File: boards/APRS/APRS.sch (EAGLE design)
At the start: 15 parts

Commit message: First pass of APRS v2
- Cleaned up the board (removed unnecessary things)
- Switched to using more library objects
- Switched to TPS6300x for power
- Integrated the Venus GPS
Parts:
- LED1: device SparkFun:LED3MM -> SparkFun-LED:LED0603
- R1, R_T0, R_T1, R_T2: device SparkFun:RESISTORAXIAL-0.3 -> SparkFun-Passives:RESISTOR0805-RES
- renumbered POWER1 to POWER5, POWER2 to POWER3
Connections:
- new net 3.3V_EN: ARDUINO.D10*, POWER3.EN
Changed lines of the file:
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@@
 <?xml version="1.0" encoding="utf-8"?>
 <!DOCTYPE eagle SYSTEM "eagle.dtd">
-<eagle version="6.1">
+<eagle version="6.2">
 <drawing>
 <settings>
@@
 <parts>
 <part name="J$1" library="SparkFun" deviceset="SMA_EDGE" device=""/>
-<part name="R_T2" library="SparkFun" deviceset="RESISTOR" device="AXIAL-0.3" value="10k"/>
-<part name="R_T1" library="SparkFun" deviceset="RESISTOR" device="AXIAL-0.3" value="10k"/>
-<part name="LED1" library="SparkFun" deviceset="LED" device="3MM"/>
-<part name="R1" library="SparkFun" deviceset="RESISTOR" device="AXIAL-0.3" value="330"/>
+<part name="R_T2" library="SparkFun-Passives" deviceset="RESISTOR" device="0805-RES" value="10k"/>
+<part name="R_T1" library="SparkFun-Passives" deviceset="RESISTOR" device="0805-RES" value="10k"/>
+<part name="LED1" library="SparkFun-LED" deviceset="LED" device="0603"/>
+<part name="R1" library="SparkFun-Passives" deviceset="RESISTOR" device="0805-RES" value="330"/>
 <part name="U$1" library="SparkFun-Aesthetics" deviceset="5V" device=""/>
 <part name="P+1" library="SparkFun-Aesthetics" deviceset="3.3V" device=""/>
@@
 <part name="GND6" library="SparkFun-Aesthetics" deviceset="GND" device=""/>
 <part name="GND7" library="SparkFun-Aesthetics" deviceset="GND" device=""/>
-<part name="R_T0" library="SparkFun" deviceset="RESISTOR" device="AXIAL-0.3" value="10k"/>
+<part name="R_T0" library="SparkFun-Passives" deviceset="RESISTOR" device="0805-RES" value="10k"/>
 <part name="THERM0" library="SparkFun" deviceset="M02" device="PTH"/>
 <part name="U$6" library="SparkFun-Aesthetics" deviceset="5V" device=""/>
@@
 <part name="THERM1" library="SparkFun-Connectors" deviceset="M02" device="JST-PTH-2"/>
 <part name="THERM2" library="SparkFun-Connectors" deviceset="M02" device="JST-PTH-2"/>
-<part name="POWER1" library="OpenSpace" deviceset="POWER" device="-TPS6300X" value="5V"/>
-<part name="POWER2" library="OpenSpace" deviceset="POWER" device="-TPS6300X" value="3.3V"/>
 <part name="RADIOMETRIX_HX1" library="OpenSpace" deviceset="RADIOMETRIX-HX1" device=""/>
 <part name="LEVEL_SHIFT" library="OpenSpace" deviceset="SN74LVC1T45" device="-DCK"/>
@@
 <part name="U$10" library="SparkFun-Aesthetics" deviceset="5V" device=""/>
 <part name="P+3" library="SparkFun-Aesthetics" deviceset="3.3V" device=""/>
+<part name="POWER5" library="OpenSpace" deviceset="POWER" device="-TPS6300X" value="5V"/>
+<part name="POWER3" library="OpenSpace" deviceset="POWER" device="-TPS6300X" value="3.3V"/>
 </parts>
 <sheets>
@@
 <instance part="GND1" gate="1" x="17.78" y="50.8"/>
 <instance part="GND2" gate="1" x="76.2" y="50.8"/>
-<instance part="U$2" gate="G$1" x="22.86" y="91.44"/>
+<instance part="U$2" gate="G$1" x="22.86" y="96.52"/>
 <instance part="GPS0" gate="G$1" x="256.54" y="22.86"/>
 <instance part="GND3" gate="1" x="99.06" y="10.16"/>
@@
 <instance part="THERM1" gate="G$1" x="218.44" y="76.2"/>
 <instance part="THERM2" gate="G$1" x="243.84" y="76.2"/>
-<instance part="POWER1" gate="POWER" x="48.26" y="83.82"/>
-<instance part="POWER2" gate="POWER" x="48.26" y="63.5"/>
 <instance part="RADIOMETRIX_HX1" gate="RADIOMETRIX-HX1_$1" x="43.18" y="33.02"/>
 <instance part="LEVEL_SHIFT" gate="G$1" x="205.74" y="25.4"/>
@@
 <instance part="U$10" gate="G$1" x="187.96" y="40.64"/>
 <instance part="P+3" gate="G$1" x="223.52" y="40.64"/>
+<instance part="POWER5" gate="POWER" x="48.26" y="83.82"/>
+<instance part="POWER3" gate="POWER" x="48.26" y="63.5"/>
 </instances>
 <busses>
@@
 </segment>
 <segment>
-<wire x1="30.48" y1="81.28" x2="17.78" y2="81.28" width="0.1524" layer="91"/>
-<wire x1="17.78" y1="81.28" x2="17.78" y2="60.96" width="0.1524" layer="91"/>
-<wire x1="17.78" y1="60.96" x2="17.78" y2="53.34" width="0.1524" layer="91"/>
-<wire x1="30.48" y1="60.96" x2="17.78" y2="60.96" width="0.1524" layer="91"/>
-<junction x="17.78" y="60.96"/>
+<wire x1="30.48" y1="78.74" x2="17.78" y2="78.74" width="0.1524" layer="91"/>
+<wire x1="17.78" y1="78.74" x2="17.78" y2="58.42" width="0.1524" layer="91"/>
+<wire x1="17.78" y1="58.42" x2="17.78" y2="53.34" width="0.1524" layer="91"/>
+<wire x1="30.48" y1="58.42" x2="17.78" y2="58.42" width="0.1524" layer="91"/>
+<junction x="17.78" y="58.42"/>
 <pinref part="GND1" gate="1" pin="GND"/>
-<pinref part="POWER1" gate="POWER" pin="BATT-"/>
-<pinref part="POWER2" gate="POWER" pin="BATT-"/>
+<pinref part="POWER5" gate="POWER" pin="BATT-"/>
+<pinref part="POWER3" gate="POWER" pin="BATT-"/>
 </segment>
 <segment>
@@
 <junction x="76.2" y="60.96"/>
 <pinref part="GND2" gate="1" pin="GND"/>
-<pinref part="POWER1" gate="POWER" pin="VCC-"/>
-<pinref part="POWER2" gate="POWER" pin="VCC-"/>
+<pinref part="POWER5" gate="POWER" pin="VCC-"/>
+<pinref part="POWER3" gate="POWER" pin="VCC-"/>
 </segment>
 <segment>
@@
 <wire x1="71.12" y1="86.36" x2="71.12" y2="91.44" width="0.1524" layer="91"/>
 <pinref part="U$1" gate="G$1" pin="5V"/>
-<pinref part="POWER1" gate="POWER" pin="VCC+"/>
+<pinref part="POWER5" gate="POWER" pin="VCC+"/>
 </segment>
 <segment>
@@
 <wire x1="71.12" y1="66.04" x2="71.12" y2="71.12" width="0.1524" layer="91"/>
 <pinref part="P+1" gate="G$1" pin="3.3V"/>
-<pinref part="POWER2" gate="POWER" pin="VCC+"/>
+<pinref part="POWER3" gate="POWER" pin="VCC+"/>
 </segment>
 <segment>
@@
 <net name="1.8V" class="0">
 <segment>
-<wire x1="30.48" y1="66.04" x2="22.86" y2="66.04" width="0.1524" layer="91"/>
-<wire x1="30.48" y1="86.36" x2="22.86" y2="86.36" width="0.1524" layer="91"/>
-<wire x1="22.86" y1="86.36" x2="22.86" y2="91.44" width="0.1524" layer="91"/>
-<wire x1="22.86" y1="66.04" x2="22.86" y2="86.36" width="0.1524" layer="91"/>
-<junction x="22.86" y="86.36"/>
+<wire x1="30.48" y1="63.5" x2="22.86" y2="63.5" width="0.1524" layer="91"/>
+<wire x1="30.48" y1="83.82" x2="22.86" y2="83.82" width="0.1524" layer="91"/>
+<wire x1="22.86" y1="83.82" x2="22.86" y2="96.52" width="0.1524" layer="91"/>
+<wire x1="22.86" y1="63.5" x2="22.86" y2="83.82" width="0.1524" layer="91"/>
+<junction x="22.86" y="83.82"/>
 <pinref part="U$2" gate="G$1" pin="1.8V"/>
-<pinref part="POWER1" gate="POWER" pin="BATT+"/>
-<pinref part="POWER2" gate="POWER" pin="BATT+"/>
+<pinref part="POWER5" gate="POWER" pin="BATT+"/>
+<pinref part="POWER3" gate="POWER" pin="BATT+"/>
 </segment>
 <segment>
@@
 </segment>
 </net>
+<net name="3.3V_EN" class="0">
+<segment>
+<pinref part="POWER3" gate="POWER" pin="EN"/>
+<wire x1="30.48" y1="68.58" x2="15.24" y2="68.58" width="0.1524" layer="91"/>
+<label x="15.24" y="68.58" size="1.778" layer="95" rot="MR0"/>
+</segment>
+<segment>
+<pinref part="ARDUINO" gate="G$1" pin="D10*"/>
+<wire x1="152.4" y1="50.8" x2="162.56" y2="50.8" width="0.1524" layer="91"/>
+<label x="162.56" y="50.8" size="1.778" layer="95"/>
+</segment>
+</net>

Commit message: New APRS board, close to ready
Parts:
- added I2C_0: (no value), SparkFun-Connectors:M04PTH
- added I2C_TRANS: PCA9306-D, OpenSpace:PCA9306-D
- added SCL_PU, SDA_PU: 3.3k, SparkFun-Passives:RESISTOR0805-RES
- ARDUINO: value ARDUINO_PRO_MINI -> ARDUINO_PRO_MINI-NOSILK; device OpenSpace:ARDUINO_PRO_MINI -> OpenSpace:ARDUINO_PRO_MINI-NOSILK
- GPS0: value VENUS_GPS -> VENUS_GPS-NOSILK; device OpenSpace:VENUS_GPS -> OpenSpace:VENUS_GPS-NOSILK
- POWER3, POWER5: device OpenSpace:POWER-TPS6300X -> OpenSpace:POWER-TPS6300X-NOSILK
- THERM0: value (none) -> 10k; device SparkFun:M02PTH -> SparkFun-Passives:RESISTOR0805-RES
- THERM1, THERM2: value (none) -> 10k
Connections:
- new net N$4: ARDUINO.A4_SDA, I2C_TRANS.SDA2
- new net N$5: ARDUINO.A5_SCL, I2C_TRANS.SCL2
- new net N$6: ARDUINO.D12, I2C_TRANS.EN
- new net SCL: I2C_0.4, I2C_TRANS.SCL1, SDA_PU.1
- new net SDA: I2C_0.3, I2C_TRANS.SDA1, SCL_PU.1
- net 3.3V: now also I2C_0.2, I2C_TRANS.VREF1, SCL_PU.2, SDA_PU.2
- net 5V: now also I2C_TRANS.VREF2, THERM0.1; no longer THERM0.2
- net A0: now also THERM0.2; no longer THERM0.1
- net GND: now also I2C_0.1, I2C_TRANS.GND
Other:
- moved on the sheet: GPS0, LEVEL_SHIFT, R_T0, R_T1, R_T2, THERM1, THERM2

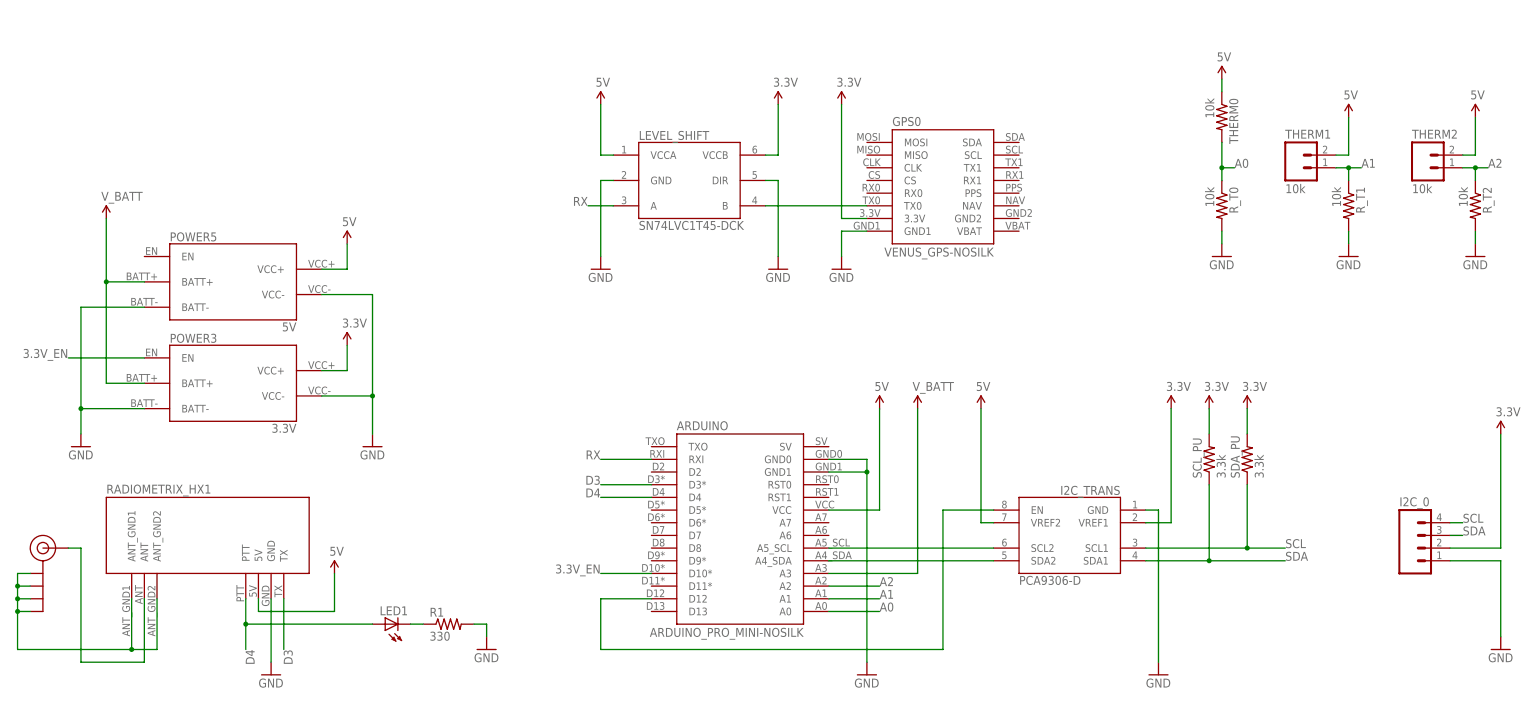
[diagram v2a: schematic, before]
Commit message: Added Jonah receiver to APRS v3
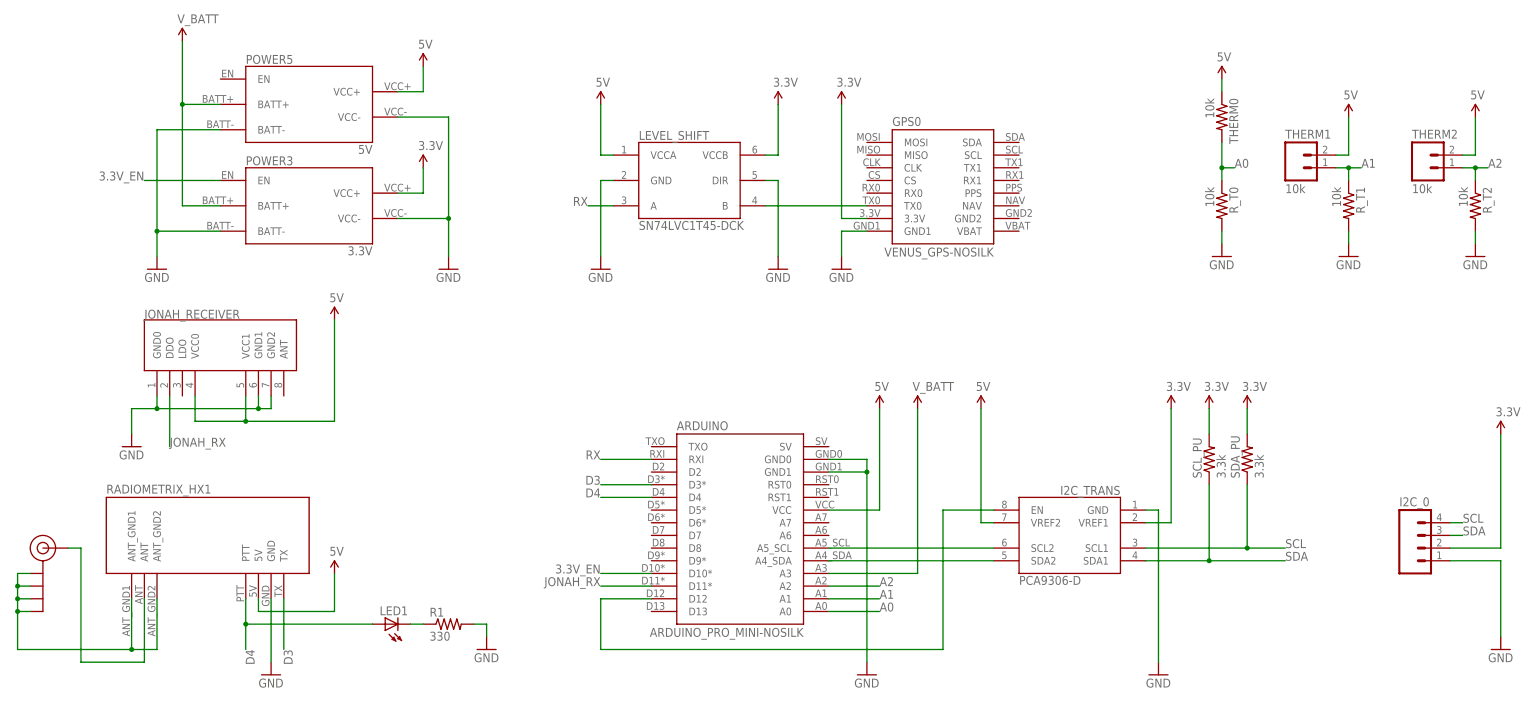
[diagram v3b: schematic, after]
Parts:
- added JONAH_RECEIVER: RADIO-KLP-RECEIVER-NOSILK, OpenSpace:RADIO-KLP-RECEIVER-NOSILK
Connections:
- new net JONAH_RX: ARDUINO.D11*, JONAH_RECEIVER.DDO
- net 5V: now also JONAH_RECEIVER.VCC0, JONAH_RECEIVER.VCC1
- net GND: now also JONAH_RECEIVER.GND0, JONAH_RECEIVER.GND1, JONAH_RECEIVER.GND2
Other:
- moved on the sheet: POWER3, POWER5
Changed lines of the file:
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@@
 <part name="P+9" library="SparkFun-Aesthetics" deviceset="3.3V" device=""/>
 <part name="GND13" library="SparkFun-Aesthetics" deviceset="GND" device=""/>
+<part name="JONAH_RECEIVER" library="OpenSpace" deviceset="RADIO-KLP-RECEIVER" device="-NOSILK"/>
+<part name="GND14" library="SparkFun-Aesthetics" deviceset="GND" device=""/>
+<part name="U$11" library="SparkFun-Aesthetics" deviceset="5V" device=""/>
 </parts>
 <sheets>
@@
 <instance part="LED1" gate="G$1" x="78.74" y="15.24" rot="R90"/>
 <instance part="R1" gate="G$1" x="91.44" y="15.24"/>
-<instance part="U$1" gate="G$1" x="71.12" y="91.44"/>
-<instance part="P+1" gate="G$1" x="71.12" y="71.12"/>
-<instance part="GND1" gate="1" x="17.78" y="50.8"/>
-<instance part="GND2" gate="1" x="76.2" y="50.8"/>
-<instance part="U$2" gate="G$1" x="22.86" y="96.52"/>
+<instance part="U$1" gate="G$1" x="86.36" y="127"/>
+<instance part="P+1" gate="G$1" x="86.36" y="106.68"/>
+<instance part="GND1" gate="1" x="33.02" y="86.36"/>
+<instance part="GND2" gate="1" x="91.44" y="86.36"/>
+<instance part="U$2" gate="G$1" x="38.1" y="132.08"/>
 <instance part="GPS0" gate="G$1" x="190.5" y="101.6"/>
 <instance part="GND3" gate="1" x="99.06" y="10.16"/>
@@
 <instance part="U$10" gate="G$1" x="121.92" y="119.38"/>
 <instance part="P+3" gate="G$1" x="157.48" y="119.38"/>
-<instance part="POWER5" gate="POWER" x="48.26" y="83.82"/>
-<instance part="POWER3" gate="POWER" x="48.26" y="63.5"/>
+<instance part="POWER5" gate="POWER" x="63.5" y="119.38"/>
+<instance part="POWER3" gate="POWER" x="63.5" y="99.06"/>
 <instance part="THERM0" gate="G$1" x="246.38" y="116.84" rot="R270"/>
 <instance part="I2C_TRANS" gate="G$1" x="215.9" y="33.02" rot="MR0"/>
@@
 <instance part="P+9" gate="G$1" x="302.26" y="53.34"/>
 <instance part="GND13" gate="1" x="302.26" y="10.16"/>
+<instance part="JONAH_RECEIVER" gate="G$1" x="45.72" y="71.12"/>
+<instance part="GND14" gate="1" x="27.94" y="50.8"/>
+<instance part="U$11" gate="G$1" x="68.58" y="76.2"/>
 </instances>
 <busses>
@@
 </segment>
 <segment>
-<wire x1="30.48" y1="78.74" x2="17.78" y2="78.74" width="0.1524" layer="91"/>
-<wire x1="17.78" y1="78.74" x2="17.78" y2="58.42" width="0.1524" layer="91"/>
-<wire x1="17.78" y1="58.42" x2="17.78" y2="53.34" width="0.1524" layer="91"/>
-<wire x1="30.48" y1="58.42" x2="17.78" y2="58.42" width="0.1524" layer="91"/>
-<junction x="17.78" y="58.42"/>
+<wire x1="45.72" y1="114.3" x2="33.02" y2="114.3" width="0.1524" layer="91"/>
+<wire x1="33.02" y1="114.3" x2="33.02" y2="93.98" width="0.1524" layer="91"/>
+<wire x1="33.02" y1="93.98" x2="33.02" y2="88.9" width="0.1524" layer="91"/>
+<wire x1="45.72" y1="93.98" x2="33.02" y2="93.98" width="0.1524" layer="91"/>
+<junction x="33.02" y="93.98"/>
 <pinref part="GND1" gate="1" pin="GND"/>
 <pinref part="POWER5" gate="POWER" pin="BATT-"/>
@@
 </segment>
 <segment>
-<wire x1="66.04" y1="81.28" x2="76.2" y2="81.28" width="0.1524" layer="91"/>
-<wire x1="76.2" y1="81.28" x2="76.2" y2="60.96" width="0.1524" layer="91"/>
-<wire x1="76.2" y1="60.96" x2="76.2" y2="53.34" width="0.1524" layer="91"/>
-<wire x1="66.04" y1="60.96" x2="76.2" y2="60.96" width="0.1524" layer="91"/>
-<junction x="76.2" y="60.96"/>
+<wire x1="81.28" y1="116.84" x2="91.44" y2="116.84" width="0.1524" layer="91"/>
+<wire x1="91.44" y1="116.84" x2="91.44" y2="96.52" width="0.1524" layer="91"/>
+<wire x1="91.44" y1="96.52" x2="91.44" y2="88.9" width="0.1524" layer="91"/>
+<wire x1="81.28" y1="96.52" x2="91.44" y2="96.52" width="0.1524" layer="91"/>
+<junction x="91.44" y="96.52"/>
 <pinref part="GND2" gate="1" pin="GND"/>
 <pinref part="POWER5" gate="POWER" pin="VCC-"/>
@@
 <pinref part="GND13" gate="1" pin="GND"/>
 </segment>
+<segment>
+<pinref part="JONAH_RECEIVER" gate="G$1" pin="GND2"/>
+<wire x1="55.88" y1="60.96" x2="55.88" y2="58.42" width="0.1524" layer="91"/>
+<wire x1="55.88" y1="58.42" x2="53.34" y2="58.42" width="0.1524" layer="91"/>
+<wire x1="53.34" y1="58.42" x2="33.02" y2="58.42" width="0.1524" layer="91"/>
+<wire x1="33.02" y1="58.42" x2="27.94" y2="58.42" width="0.1524" layer="91"/>
+<wire x1="27.94" y1="58.42" x2="27.94" y2="53.34" width="0.1524" layer="91"/>
+<pinref part="JONAH_RECEIVER" gate="G$1" pin="GND1"/>
+<wire x1="53.34" y1="60.96" x2="53.34" y2="58.42" width="0.1524" layer="91"/>
+<junction x="53.34" y="58.42"/>
+<pinref part="JONAH_RECEIVER" gate="G$1" pin="GND0"/>
+<wire x1="33.02" y1="60.96" x2="33.02" y2="58.42" width="0.1524" layer="91"/>
+<junction x="33.02" y="58.42"/>
+<pinref part="GND14" gate="1" pin="GND"/>
+</segment>
 </net>
 <net name="RX" class="0">
@@
 </segment>
 <segment>
-<wire x1="66.04" y1="86.36" x2="71.12" y2="86.36" width="0.1524" layer="91"/>
-<wire x1="71.12" y1="86.36" x2="71.12" y2="91.44" width="0.1524" layer="91"/>
+<wire x1="81.28" y1="121.92" x2="86.36" y2="121.92" width="0.1524" layer="91"/>
+<wire x1="86.36" y1="121.92" x2="86.36" y2="127" width="0.1524" layer="91"/>
 <pinref part="U$1" gate="G$1" pin="5V"/>
 <pinref part="POWER5" gate="POWER" pin="VCC+"/>
@@
 <wire x1="198.12" y1="35.56" x2="198.12" y2="58.42" width="0.1524" layer="91"/>
 </segment>
+<segment>
+<pinref part="JONAH_RECEIVER" gate="G$1" pin="VCC0"/>
+<wire x1="40.64" y1="60.96" x2="40.64" y2="55.88" width="0.1524" layer="91"/>
+<wire x1="40.64" y1="55.88" x2="50.8" y2="55.88" width="0.1524" layer="91"/>
+<wire x1="50.8" y1="55.88" x2="68.58" y2="55.88" width="0.1524" layer="91"/>
+<wire x1="68.58" y1="55.88" x2="68.58" y2="76.2" width="0.1524" layer="91"/>
+<pinref part="JONAH_RECEIVER" gate="G$1" pin="VCC1"/>
+<wire x1="50.8" y1="60.96" x2="50.8" y2="55.88" width="0.1524" layer="91"/>
+<junction x="50.8" y="55.88"/>
+<pinref part="U$11" gate="G$1" pin="5V"/>
+</segment>
 </net>
 <net name="N$11" class="0">
@@
 <net name="3.3V" class="0">
 <segment>
-<wire x1="66.04" y1="66.04" x2="71.12" y2="66.04" width="0.1524" layer="91"/>
-<wire x1="71.12" y1="66.04" x2="71.12" y2="71.12" width="0.1524" layer="91"/>
+<wire x1="81.28" y1="101.6" x2="86.36" y2="101.6" width="0.1524" layer="91"/>
+<wire x1="86.36" y1="101.6" x2="86.36" y2="106.68" width="0.1524" layer="91"/>
 <pinref part="P+1" gate="G$1" pin="3.3V"/>
 <pinref part="POWER3" gate="POWER" pin="VCC+"/>
@@
 <net name="1.8V" class="0">
 <segment>
-<wire x1="30.48" y1="63.5" x2="22.86" y2="63.5" width="0.1524" layer="91"/>
-<wire x1="30.48" y1="83.82" x2="22.86" y2="83.82" width="0.1524" layer="91"/>
-<wire x1="22.86" y1="83.82" x2="22.86" y2="96.52" width="0.1524" layer="91"/>
-<wire x1="22.86" y1="63.5" x2="22.86" y2="83.82" width="0.1524" layer="91"/>
-<junction x="22.86" y="83.82"/>
+<wire x1="45.72" y1="99.06" x2="38.1" y2="99.06" width="0.1524" layer="91"/>
+<wire x1="45.72" y1="119.38" x2="38.1" y2="119.38" width="0.1524" layer="91"/>
+<wire x1="38.1" y1="119.38" x2="38.1" y2="132.08" width="0.1524" layer="91"/>
+<wire x1="38.1" y1="99.06" x2="38.1" y2="119.38" width="0.1524" layer="91"/>
+<junction x="38.1" y="119.38"/>
 <pinref part="U$2" gate="G$1" pin="1.8V"/>
 <pinref part="POWER5" gate="POWER" pin="BATT+"/>
@@
 <segment>
 <pinref part="POWER3" gate="POWER" pin="EN"/>
-<wire x1="30.48" y1="68.58" x2="15.24" y2="68.58" width="0.1524" layer="91"/>
-<label x="15.24" y="68.58" size="1.778" layer="95" rot="MR0"/>
+<wire x1="45.72" y1="104.14" x2="30.48" y2="104.14" width="0.1524" layer="91"/>
+<label x="30.48" y="104.14" size="1.778" layer="95" rot="MR0"/>
 </segment>
 <segment>
@@
 </segment>
 </net>
+<net name="JONAH_RX" class="0">
+<segment>
+<pinref part="ARDUINO" gate="G$1" pin="D11*"/>
+<wire x1="132.08" y1="22.86" x2="121.92" y2="22.86" width="0.1524" layer="91"/>
+<label x="121.92" y="22.86" size="1.778" layer="95" rot="MR0"/>
+</segment>
+<segment>
+<pinref part="JONAH_RECEIVER" gate="G$1" pin="DDO"/>
+<wire x1="35.56" y1="60.96" x2="35.56" y2="50.8" width="0.1524" layer="91"/>
+<label x="35.56" y="50.8" size="1.778" layer="95"/>
+</segment>
+</net>
